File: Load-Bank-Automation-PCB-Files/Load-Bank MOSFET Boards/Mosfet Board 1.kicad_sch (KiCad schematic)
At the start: 26 parts, among them J2 Conn_01x03, J22 Conn_01x03, Q22 GSGN0648, Q3 GSGN0648, U10 MCP6006-OTVAO, U7 ACS711KEXLT-31AB-T, U8 IRS10752LTRPBF

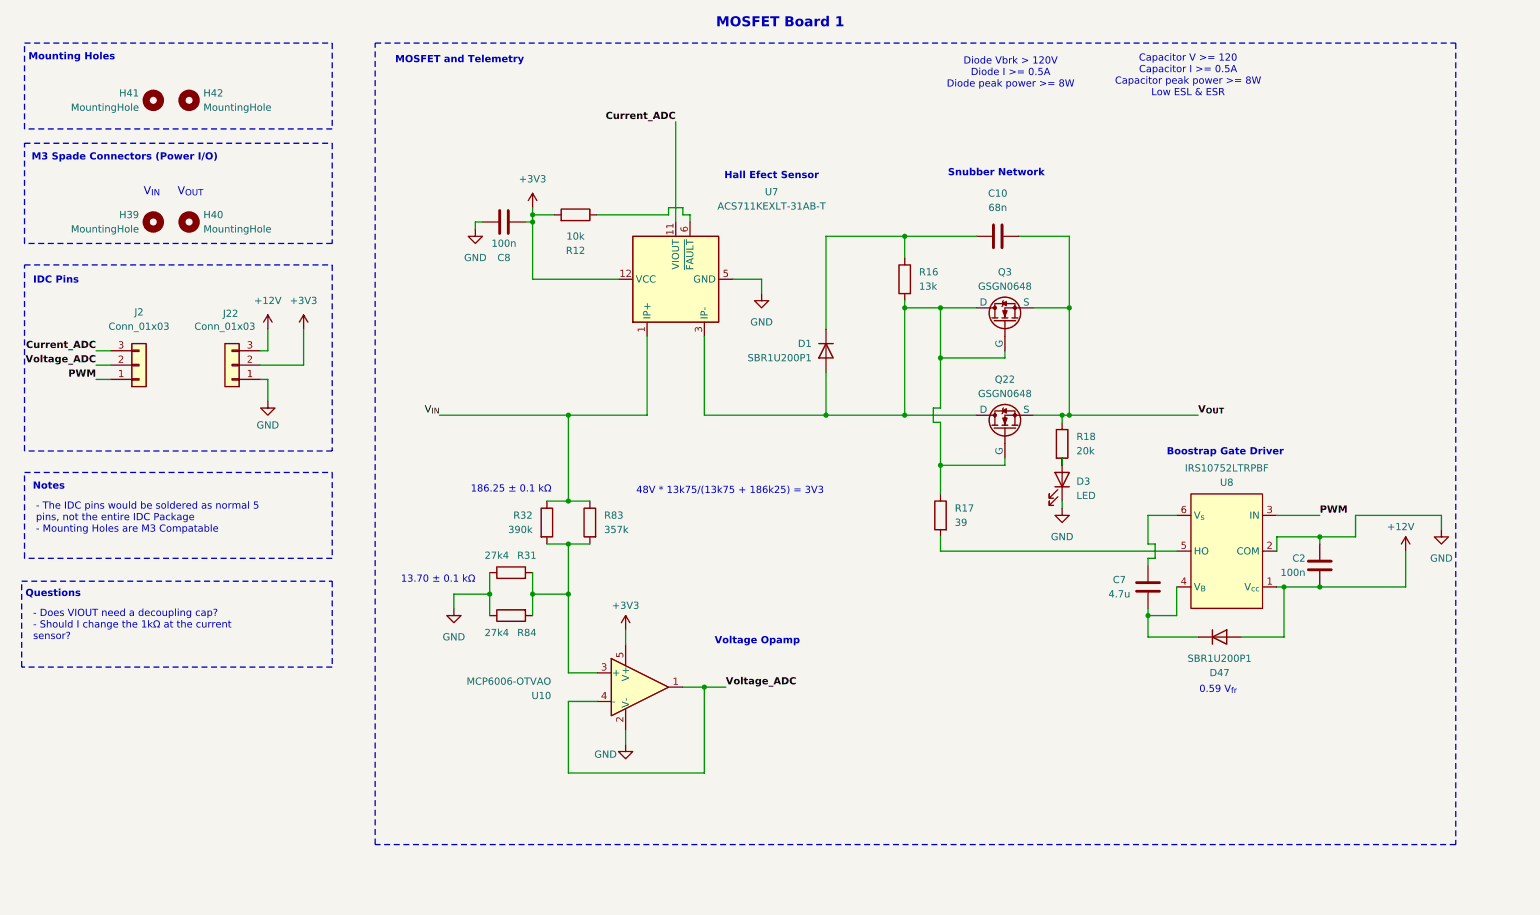
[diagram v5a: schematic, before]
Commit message: MOSFET Board Layout is good
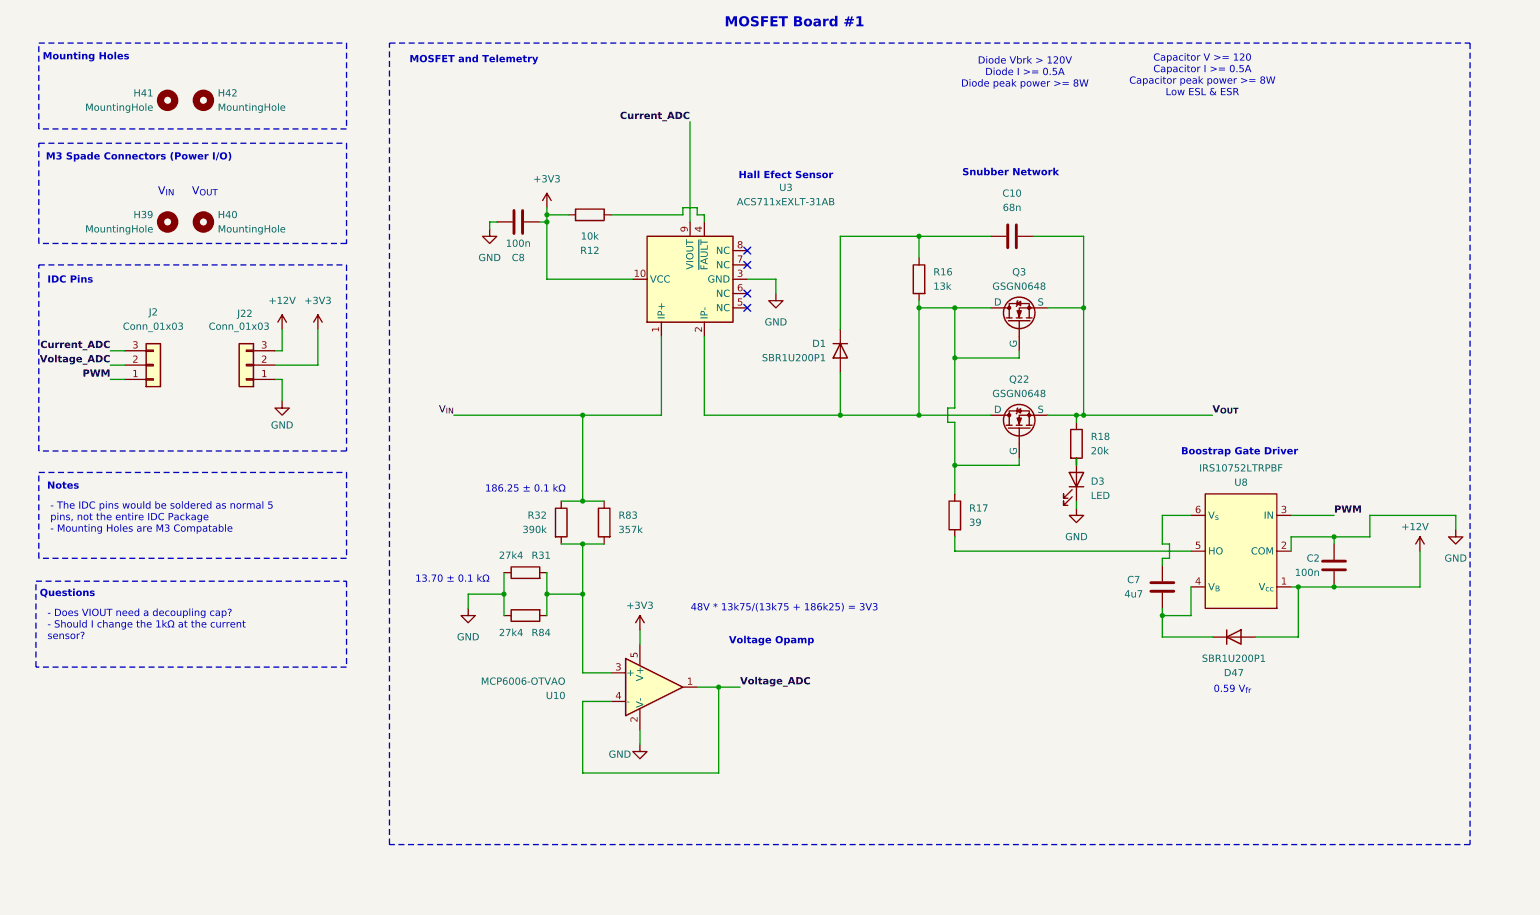
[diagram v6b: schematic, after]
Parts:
- removed U7: ACS711KEXLT-31AB-T, Package_DFN_QFN:XDCR_ACS711KEXLT-15AB-T, symbol Sensor_Current:ACS711xLCTR-25AB
- added U3: ACS711xEXLT-31AB, Sensor_Current:Allegro_QFN-12-10-1EP_3x3mm_P0.5mm, symbol Sensor_Current:ACS711xEXLT-31AB
- C7: value 4.7u -> 4u7
- C8: footprint Capacitor_SMD:C_1206_3216Metric_Pad1.33x1.80mm_HandSolder -> Capacitor_SMD:C_0603_1608Metric_Pad1.08x0.95mm_HandSolder
- J2, J22: footprint Connector_PinHeader_1.00mm:IDC_PinHeader_1x03_P1.00mm_Vertical -> Connector_IDC:IDC-Header_1x03_P2.54mm_Vertical
- Q22, Q3: footprint Package_TO_SOT_SMD:Goodarksemiconductor_PPAK_3x3 -> Package_SO:PPAK 3x3
- R12, R18: footprint Resistor_SMD:R_1206_3216Metric_Pad1.30x1.75mm_HandSolder -> Resistor_SMD:R_1210_3225Metric_Pad1.30x2.65mm_HandSolder
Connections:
- net +3V3: now also U3.10 (VCC)
- net Current_ADC: now also U3.9 (VIOUT)
- net GND: now also U3.3 (GND)
- net V_{IN}: now also U3.1 (IP+)
- net at D1.2 (A), Q22.1 (D), Q22.2 (G)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: now also U3.2 (IP-)
- net at R12.1: now also U3.4 (~{FAULT})
- no-connect marks 0 -> 4
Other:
- note added: "MOSFET Board #1"
- note removed: "MOSFET Board 1"
